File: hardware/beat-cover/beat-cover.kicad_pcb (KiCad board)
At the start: 2 copper layers, 60 x 35 mm, 13 parts

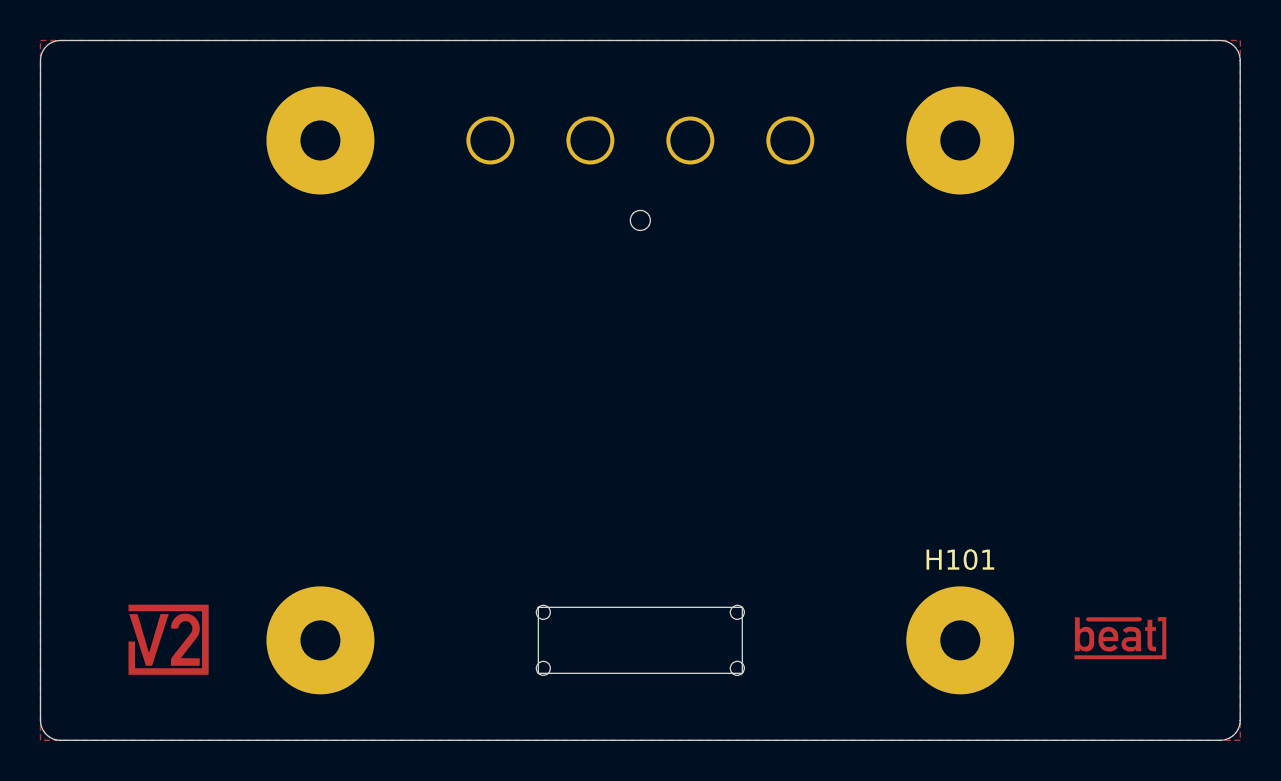
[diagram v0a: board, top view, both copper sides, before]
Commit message: Replace Order_Number
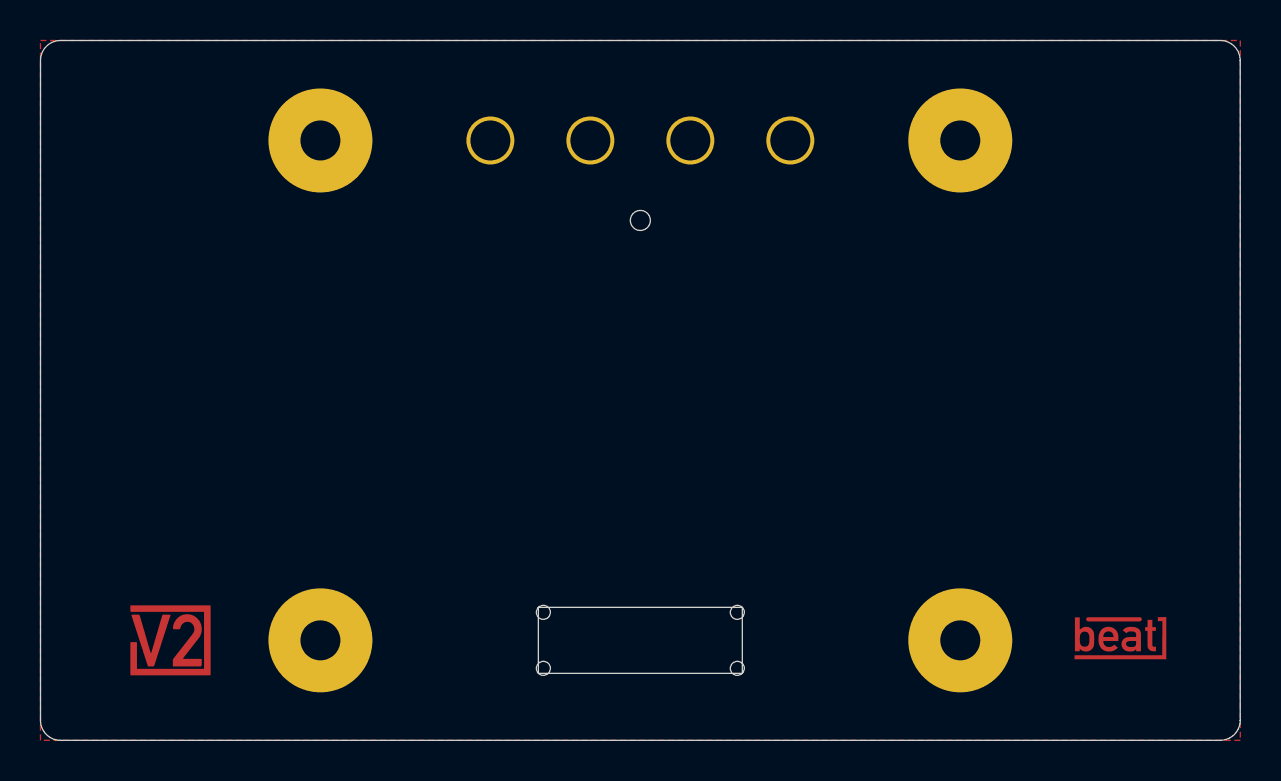
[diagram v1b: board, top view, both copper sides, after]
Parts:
- H101, H102, H103, H104: value MountingHole_2mm_Pad_5.2mm -> 2mm_Pad_5.2mm
- H105: value MountingHole_1mm -> 1mm
- H106, H107, H108, H109: value MountingHole_2mm_Pad_2.4mm -> 2mm_Pad_2.4mm
- INFO101: value ORDER-NUMBER -> ~; footprint V2_Production:Order_Number -> V2_Production:Revision
